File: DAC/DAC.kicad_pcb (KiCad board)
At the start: 4 copper layers, 42 parts, among them J1 Conn_01x06, J2 Conn_01x06, J3 Conn_01x02_Male-I2C, SW1 SW_Push, U1 TPS73633DBV, U2 PCM5242RHB

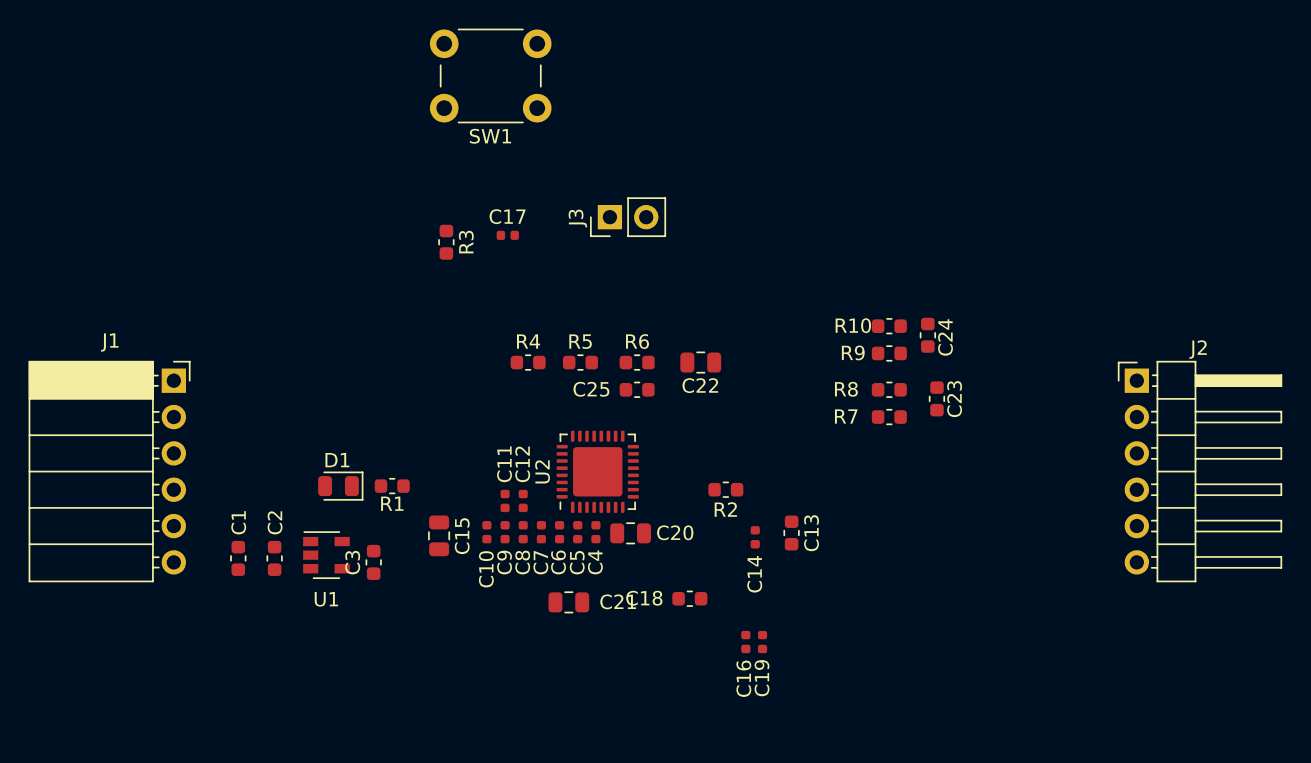
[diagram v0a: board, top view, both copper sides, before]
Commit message: Added first pass at routing the DAC PCB
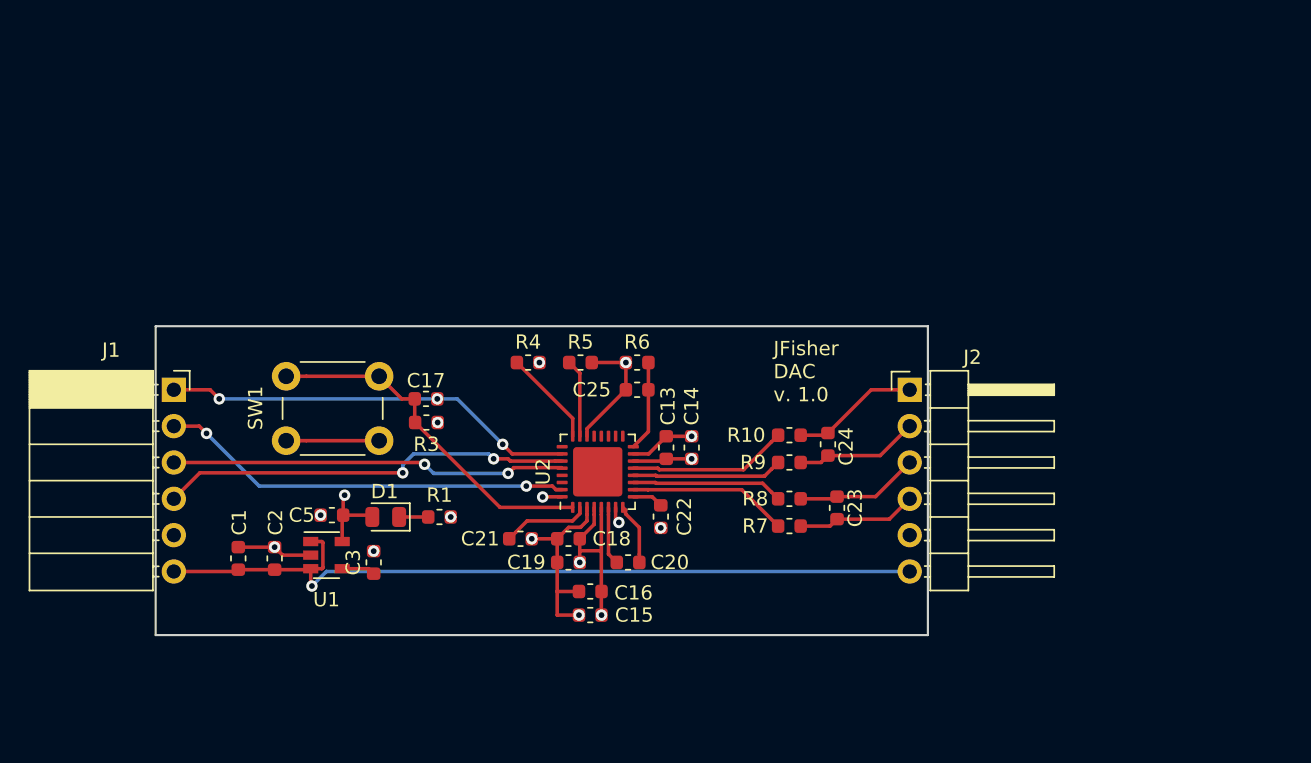
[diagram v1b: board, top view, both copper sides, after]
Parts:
- removed C10, C11, C12, C6, C7, C8, C9: 0.1uF, Capacitor_SMD:C_0402_1005Metric
- removed C4: 10uF, Capacitor_SMD:C_0402_1005Metric
- removed J3: Conn_01x02_Male-I2C, Connector_PinHeader_2.54mm:PinHeader_1x02_P2.54mm_Vertical
- removed R2: 10, Resistor_SMD:R_0603_1608Metric
- C14, C16, C17, C19, C5: footprint Capacitor_SMD:C_0402_1005Metric -> Capacitor_SMD:C_0603_1608Metric
- C15, C20, C21, C22: footprint Capacitor_SMD:C_0805_2012Metric -> Capacitor_SMD:C_0603_1608Metric
- moved SW1 25.7 mm to (127.4, 48.6)
- moved C5 17.2 mm to (124.1, 53.8), turned to 180 degrees
- moved J2 15.9 mm to (164.5, 45.1)
- moved C19 14.7 mm to (140.6, 57.1), turned to 180 degrees
- moved C17 12.8 mm to (130.7, 45.7)
- moved R3 12.7 mm to (130.7, 47.4), turned to 0 degrees
- moved C15 11.9 mm to (142.1, 60.8), turned to 180 degrees
- moved C16 11.4 mm to (142.1, 59.2), turned to 180 degrees
- moved C22 11.1 mm to (147.1, 53.9), turned to 270 degrees
- moved C13 10.6 mm to (147.4, 49.1), turned to 90 degrees
- moved C23 10.3 mm to (159.4, 53.3)
- moved C24 10.3 mm to (158.8, 48.9)
- moved R10 10.3 mm to (156.1, 48.3)
- moved R7 10.3 mm to (156.1, 54.6)
- moved R8 10.3 mm to (156.1, 52.7)
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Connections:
- C13 pad 1: Net-(C13-Pad1) -> +3V3
- C14 pad 1: Net-(C13-Pad1) -> +3V3
- J2 pad 1: DACL+ -> DACR+
- J2 pad 2: DACL- -> DACR-
- J2 pad 3: DACR+ -> DACL-
- J2 pad 4: DACR- -> DACL+
- U2 pad 14: Net-(C13-Pad1) -> +3V3
- U2 pad 17: Net-(J3-Pad2) -> (no net)
- U2 pad 18: Net-(J3-Pad1) -> (no net)
- U2 pad 19: Net-(U2-Pad19) -> (no net)
- U2 pad 20: Net-(U2-Pad20) -> (no net)
- U2 pad 21: Net-(U2-Pad21) -> (no net)
- U2 pad 25: Net-(U2-Pad25) -> (no net)
- U2 pad 29: Net-(U2-Pad29) -> (no net)
- U2 pad 30: Net-(U2-Pad30) -> (no net)
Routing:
- net VUSB: track 0.00 -> 56.6 mm, vias 0 -> 1
- net GND: track 0.00 -> 41.3 mm, vias 0 -> 14
- net I2S_MCLK: track 0.00 -> 29.0 mm, vias 0 -> 2
- net I2S_LRCK: track 0.00 -> 29.0 mm, vias 0 -> 2
- net I2S_SCLK: track 0.00 -> 29.0 mm, vias 0 -> 2
- net I2S_DIN: track 0.00 -> 27.6 mm, vias 0 -> 2
- net Net-(C17-Pad1): track 0.00 -> 24.8 mm
- net +3V3: track 0.00 -> 22.9 mm, vias 0 -> 6
- net Net-(R7-Pad2): track 0.00 -> 11.2 mm
- net Net-(R10-Pad2): track 0.00 -> 11.2 mm
- net Net-(R8-Pad2): track 0.00 -> 10.6 mm
- net Net-(R9-Pad2): track 0.00 -> 10.5 mm
- net DACR+: track 0.00 -> 8.94 mm
- net DACR-: track 0.00 -> 8.67 mm
- net DACL-: track 0.00 -> 8.67 mm
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- added copper zone on In2.Cu, net +3V3
- added copper zone on In1.Cu, net GND
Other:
- board outline added: 54 x 21.6 mm
- board text added: "JFisher DAC v. 1.0"

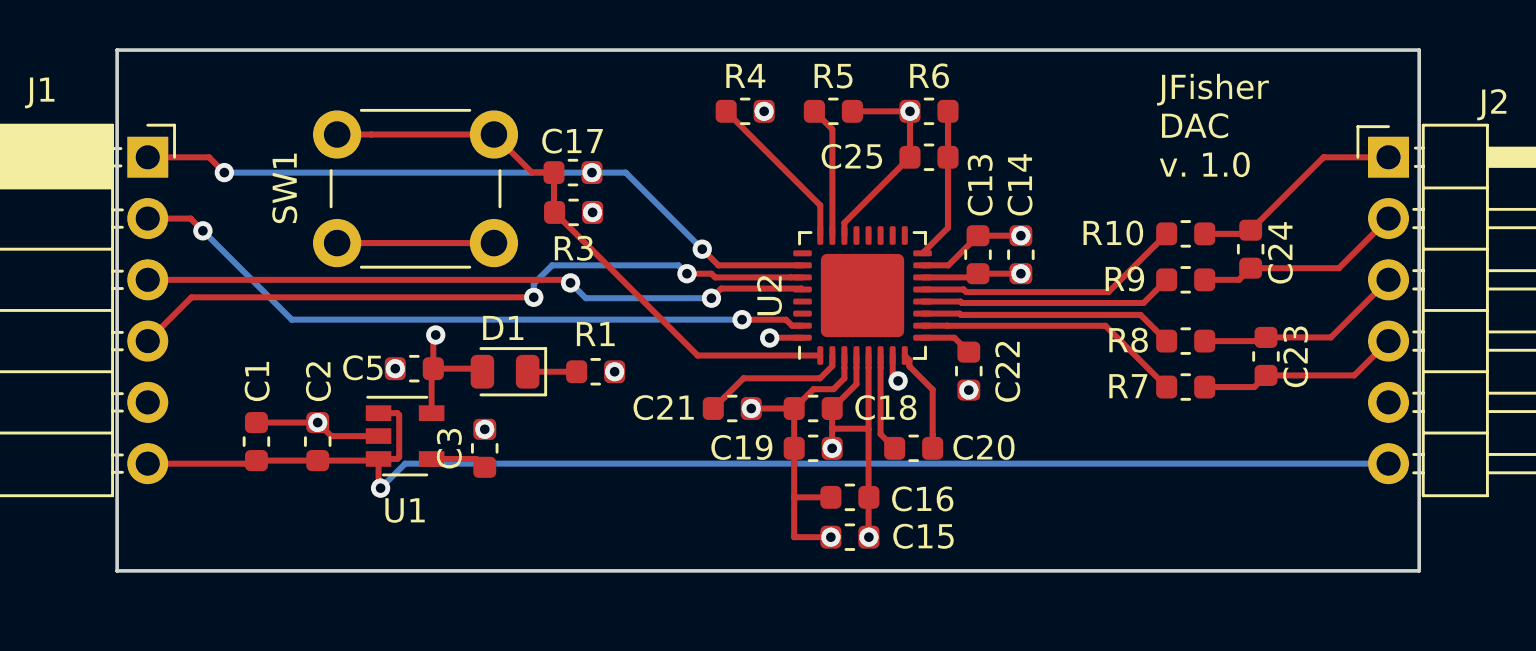
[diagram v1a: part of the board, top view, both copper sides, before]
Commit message: Update routing of DAC board
- Route differential outputs with matching lengths
- Add silkscreen labels for inputs and outputs
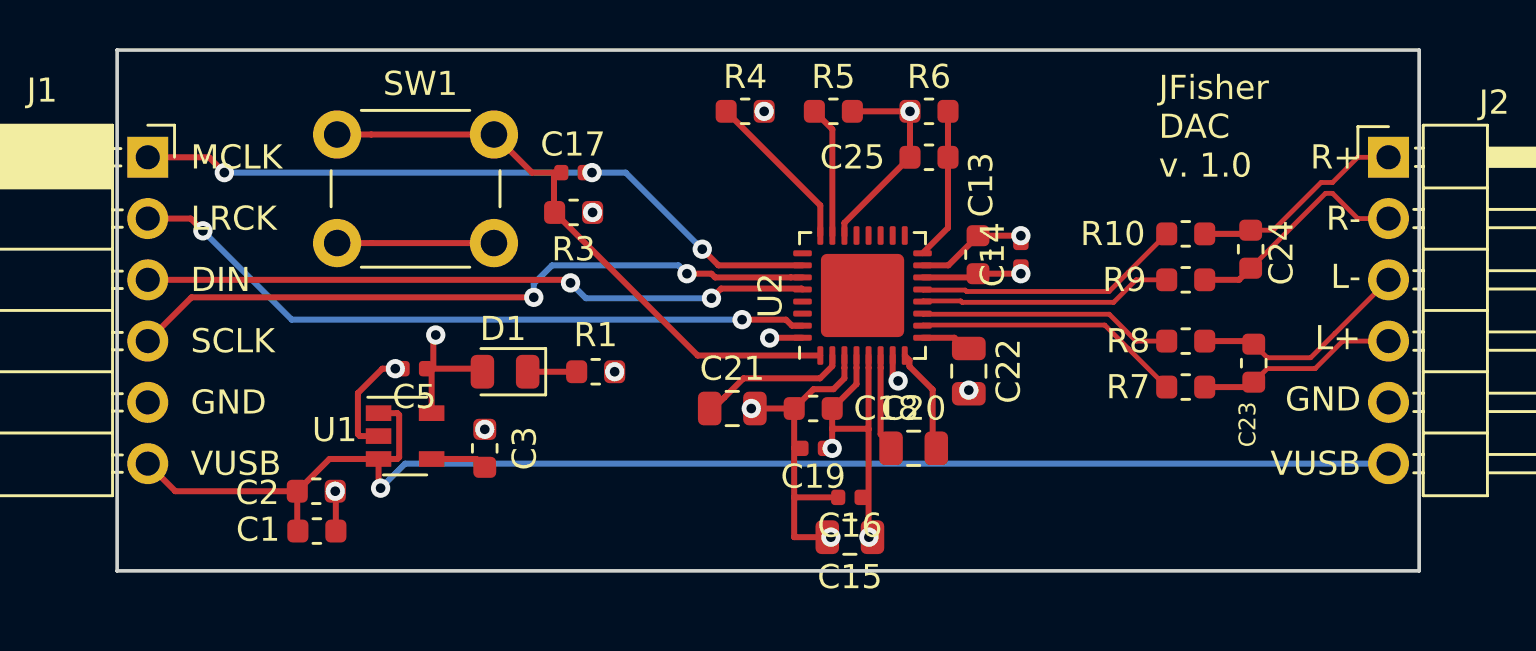
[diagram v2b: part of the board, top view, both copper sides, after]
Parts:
- C14, C16, C17, C19, C5: footprint Capacitor_SMD:C_0603_1608Metric -> Capacitor_SMD:C_0402_1005Metric
- C15, C20, C21, C22: footprint Capacitor_SMD:C_0603_1608Metric -> Capacitor_SMD:C_0805_2012Metric
- moved C1 4.48 mm to (120.0, 60.6), turned to 0 degrees
- moved C2 2.06 mm to (120.0, 58.9), turned to 0 degrees
- moved C23 0.58 mm to (158.9, 53.6)
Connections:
- net Net-(R10-Pad2) renamed OUTR_P
- net Net-(R7-Pad2) renamed OUTL_P
- net Net-(R8-Pad2) renamed OUTL_N
- net Net-(R9-Pad2) renamed OUTR_N
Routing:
- net VUSB: track 56.6 -> 59.2 mm
- net GND: track 41.3 -> 42.2 mm
- net DACR-: track 8.67 -> 9.54 mm
- net DACL-: track 8.67 -> 9.24 mm
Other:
- board text added: "DIN"
- board text added: "GND"
- board text added: "L+"
- board text added: "L-"
- board text added: "LRCK"
- board text added: "MCLK"
- board text added: "R+"
- board text added: "R-"
- board text added: "SCLK"
- board text added: "VUSB"

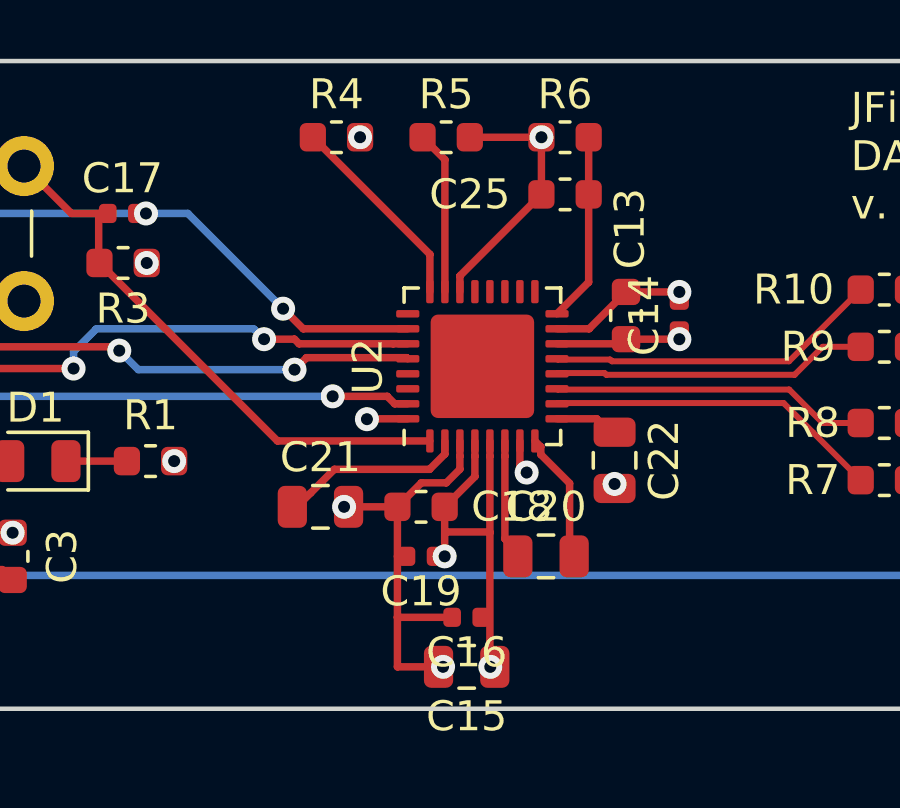
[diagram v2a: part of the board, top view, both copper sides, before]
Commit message: Updated routing information & silk screens
- Update pin names of differential outputs of PCM5242
- Better alignment of silkscreen component labels
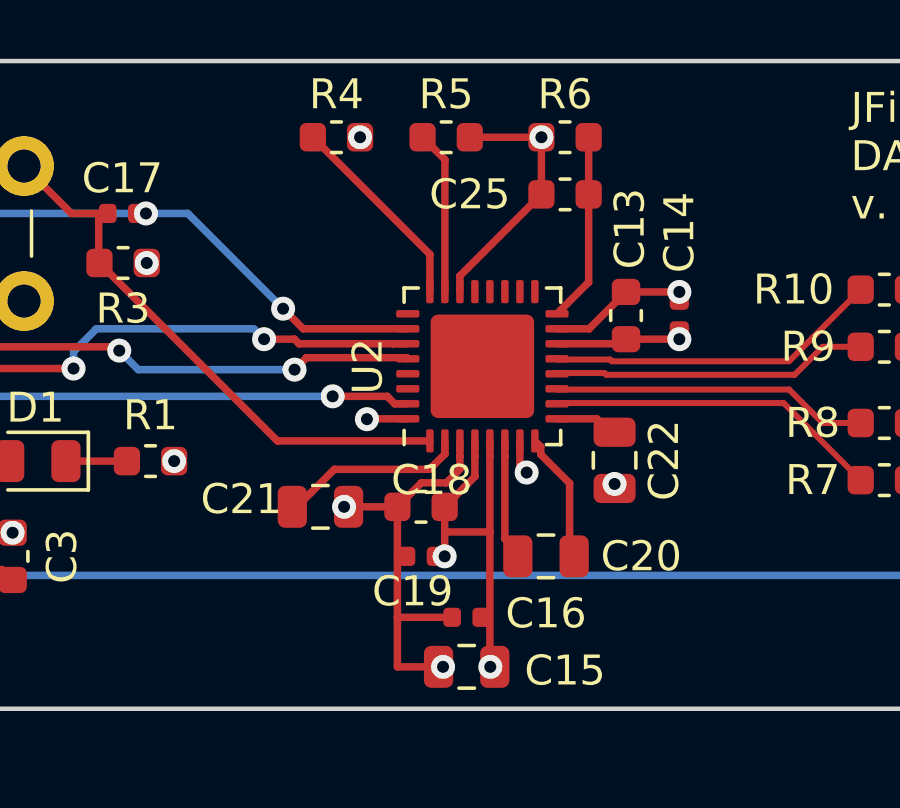
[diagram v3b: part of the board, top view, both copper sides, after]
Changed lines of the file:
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@@
     (tags capacitor)
     (attr smd)
-    (fp_text reference C18 (at -3.0225 0 180) (layer F.SilkS)
+    (fp_text reference C18 (at -0.3555 0.889 180) (layer F.SilkS)
       (effects (font (size 1 1) (thickness 0.15)))
     )
@@
     (tags capacitor)
     (attr smd)
-    (fp_text reference C14 (at 0 -1.17 90) (layer F.SilkS)
+    (fp_text reference C14 (at 2.7685 0 90) (layer F.SilkS)
       (effects (font (size 1 1) (thickness 0.15)))
     )
@@
     (tags capacitor)
     (attr smd)
-    (fp_text reference C15 (at 0 -1.65 180) (layer F.SilkS)
+    (fp_text reference C15 (at -3.279 -0.127 180) (layer F.SilkS)
       (effects (font (size 1 1) (thickness 0.15)))
     )
@@
     (tags capacitor)
     (attr smd)
-    (fp_text reference C16 (at 0 -1.17 180) (layer F.SilkS)
+    (fp_text reference C16 (at -2.644 0.127 180) (layer F.SilkS)
       (effects (font (size 1 1) (thickness 0.15)))
     )
@@
     (tags capacitor)
     (attr smd)
-    (fp_text reference C19 (at 0 -1.17 180) (layer F.SilkS)
+    (fp_text reference C19 (at 0.2795 -1.17 180) (layer F.SilkS)
       (effects (font (size 1 1) (thickness 0.15)))
     )
@@
     (tags capacitor)
     (attr smd)
-    (fp_text reference C20 (at 0 -1.65) (layer F.SilkS)
+    (fp_text reference C20 (at 3.175 0) (layer F.SilkS)
       (effects (font (size 1 1) (thickness 0.15)))
     )
@@
     (tags capacitor)
     (attr smd)
-    (fp_text reference C21 (at 0 -1.65) (layer F.SilkS)
-      (effects (font (size 1 1) (thickness 0.15)))
-    )
+    (fp_text reference C21 (at -2.6415 -0.254) (layer F.SilkS)
+      (effects (font (size 1 1) (thickness 0.15)))
+    )

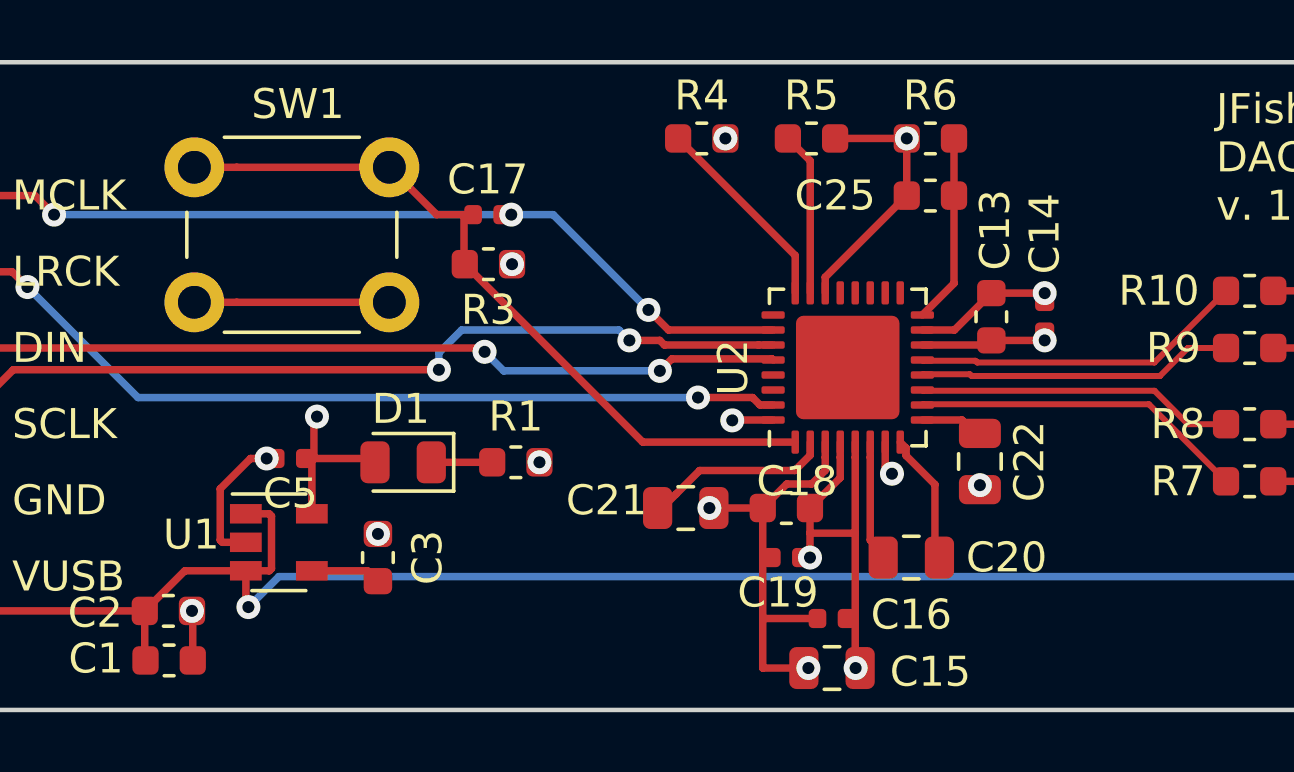
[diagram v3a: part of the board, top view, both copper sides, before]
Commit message: Convert blind vias to through and update DAC layout
This will constitute the first spin of the DAC board.
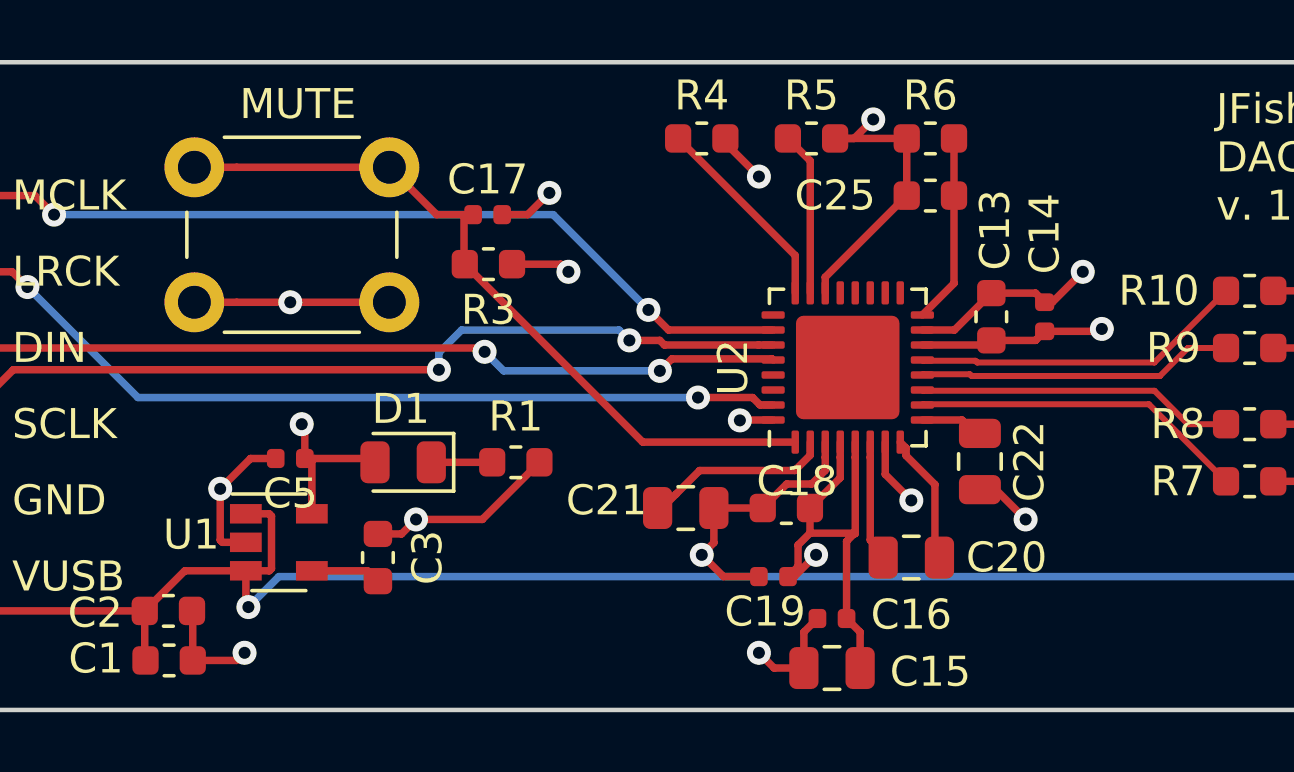
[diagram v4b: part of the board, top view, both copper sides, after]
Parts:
- moved C19 0.77 mm to (140.2, 57.8)
- renumbered SW1 to MUTE
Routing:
- net GND: track 42.2 -> 57.5 mm, vias 14 -> 12
- net +3V3: track 22.9 -> 30.9 mm, vias 6 -> 5
